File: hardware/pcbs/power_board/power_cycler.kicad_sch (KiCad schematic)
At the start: 6 parts, among them J22 ScrewTerminal_02, Q5 IRFR5305

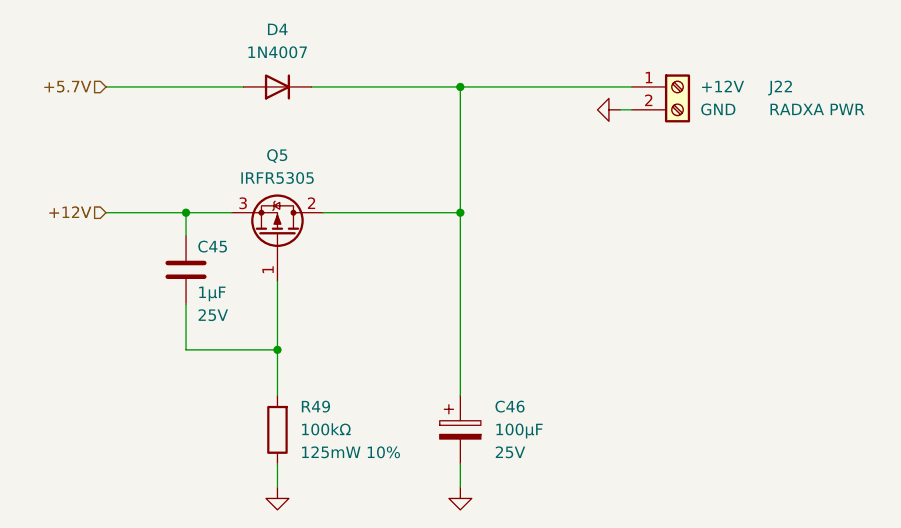
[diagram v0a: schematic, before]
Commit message: power_board: finalise isolated chargers and place USB3 passthrough
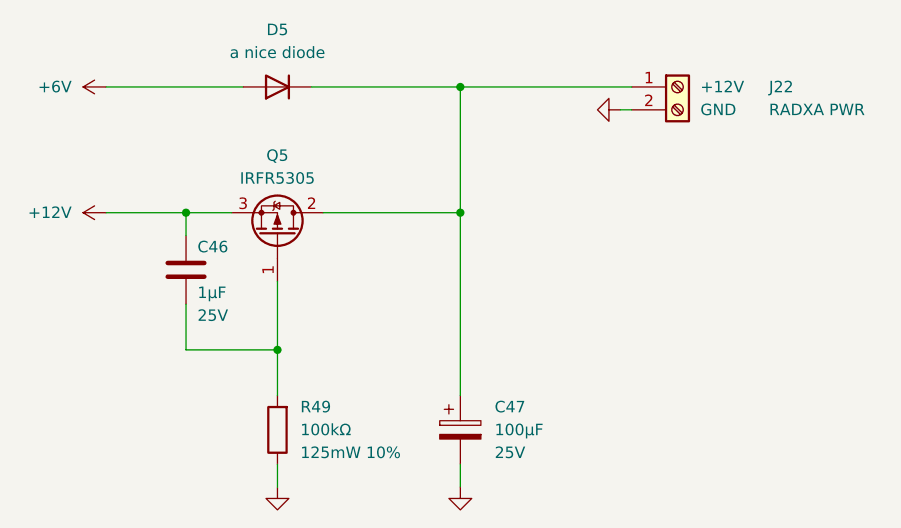
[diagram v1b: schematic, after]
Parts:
- D5: renamed from D4; value 1N4007 -> a nice diode; footprint Diode_THT:D_DO-41_SOD81_P10.16mm_Horizontal -> Diode_SMD:D_SMC; Shop (none) -> TODO
- renumbered C45 to C46, C46 to C47
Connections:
- net +5.7V renamed +6V
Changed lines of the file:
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@@
-		)
-	)
-	(hierarchical_label "+5.7V"
-		(shape input)
-		(at 110.49 71.12 180)
-		(fields_autoplaced yes)
-		(effects
-			(font
-				(size 1.27 1.27)
-			)
-			(justify right)
-		)
-	)
-	(hierarchical_label "+12V"
-		(shape input)
-		(at 110.49 85.09 180)
-		(fields_autoplaced yes)
-		(effects
-			(font
-				(size 1.27 1.27)
-			)
-			(justify right)
 		)
 	)
@@
 		(on_board yes)
 		(dnp no)
-		(property "Reference" "C45"
+		(property "Reference" "C46"
 			(at 120.65 88.9 0)
 			(effects
@@
 			(project "power_board"
 				(path "/4b166175-80a4-48c6-994d-6e62a6160b87/bf145c4c-69aa-4291-854e-cae968acbb49"
-					(reference "C45")
+					(reference "C46")
 					(unit 1)
 				)
@@
 		(dnp no)
 		(fields_autoplaced yes)
-		(property "Reference" "#PWR0111"
+		(property "Reference" "#PWR0110"
 			(at 161.29 73.66 0)
 			(effects
@@
 			(project "power_board"
 				(path "/4b166175-80a4-48c6-994d-6e62a6160b87/bf145c4c-69aa-4291-854e-cae968acbb49"
-					(reference "#PWR0111")
+					(reference "#PWR0110")
 					(unit 1)
 				)
@@
 		(dnp no)
 		(fields_autoplaced yes)
-		(property "Reference" "#PWR0109"
+		(property "Reference" "#PWR0108"
 			(at 129.54 121.92 0)
 			(effects
@@
 			(project "power_board"
 				(path "/4b166175-80a4-48c6-994d-6e62a6160b87/bf145c4c-69aa-4291-854e-cae968acbb49"
-					(reference "#PWR0109")
+					(reference "#PWR0108")
 					(unit 1)
 				)
@@
 		(dnp no)
 		(fields_autoplaced yes)
-		(property "Reference" "D4"
+		(property "Reference" "D5"
 			(at 129.54 64.77 0)
 			(effects
@@
 			)
 		)
-		(property "Value" "1N4007"
+		(property "Value" "a nice diode"
 			(at 129.54 67.31 0)
 			(effects
@@
 			)
 		)
-		(property "Footprint" "Diode_THT:D_DO-41_SOD81_P10.16mm_Horizontal"
+		(property "Footprint" "Diode_SMD:D_SMC"
 			(at 129.54 66.675 0)
 			(effects
@@
 			)
 		)
+		(property "Shop" "TODO"
+			(at 129.54 71.12 0)
+			(effects
+				(font
+					(size 1.27 1.27)
+				)
+				(hide yes)
+			)
+		)
 		(pin "2"
 		)
@@
 			(project "power_board"
 				(path "/4b166175-80a4-48c6-994d-6e62a6160b87/bf145c4c-69aa-4291-854e-cae968acbb49"
-					(reference "D4")
+					(reference "D5")
 					(unit 1)
 				)
@@
 		(on_board yes)
 		(dnp no)
-		(property "Reference" "C46"
+		(property "Reference" "C47"
 			(at 153.67 106.68 0)
 			(effects
@@
 			(project "power_board"
 				(path "/4b166175-80a4-48c6-994d-6e62a6160b87/bf145c4c-69aa-4291-854e-cae968acbb49"
-					(reference "C46")
+					(reference "C47")
 					(unit 1)
 				)
@@
 		(dnp no)
 		(fields_autoplaced yes)
-		(property "Reference" "#PWR0110"
+		(property "Reference" "#PWR0109"
 			(at 149.86 121.92 0)
 			(effects
@@
 			(project "power_board"
 				(path "/4b166175-80a4-48c6-994d-6e62a6160b87/bf145c4c-69aa-4291-854e-cae968acbb49"
-					(reference "#PWR0110")
+					(reference "#PWR0109")
+					(unit 1)
+				)
+			)
+		)
+	)
+	(symbol
+		(lib_id "power:+12V")
+		(at 110.49 85.09 90)
+		(unit 1)
+		(exclude_from_sim no)
+		(in_bom yes)
+		(on_board yes)
+		(dnp no)
+		(fields_autoplaced yes)
+		(property "Reference" "#PWR0107"
+			(at 114.3 85.09 0)
+			(effects
+				(font
+					(size 1.27 1.27)
+				)
+				(hide yes)
+			)
+		)
+		(property "Value" "+12V"
+			(at 106.68 85.0899 90)
+			(effects
+				(font
+					(size 1.27 1.27)
+				)
+				(justify left)
+			)
+		)
+		(property "Footprint" ""
+			(at 110.49 85.09 0)
+			(effects
+				(font
+					(size 1.27 1.27)
+				)
+				(hide yes)
+			)
+		)
+		(property "Datasheet" ""
+			(at 110.49 85.09 0)
+			(effects
+				(font
+					(size 1.27 1.27)
+				)
+				(hide yes)
+			)
+		)
+		(property "Description" "Power symbol creates a global label with name \"+12V\""
+			(at 110.49 85.09 0)
+			(effects
+				(font
+					(size 1.27 1.27)
+				)
+				(hide yes)
+			)
+		)
+		(pin "1"
+		)
+		(instances
+			(project "power_board"
+				(path "/4b166175-80a4-48c6-994d-6e62a6160b87/bf145c4c-69aa-4291-854e-cae968acbb49"
+					(reference "#PWR0107")
 					(unit 1)
 				)
@@
 					(unit 1)
 				)
+			)
+		)
+	)
+	(symbol
+		(lib_id "power:+6V")
+		(at 110.49 71.12 90)
+		(unit 1)
+		(exclude_from_sim no)
+		(in_bom yes)
+		(on_board yes)
+		(dnp no)
+		(fields_autoplaced yes)
+		(property "Reference" "#PWR0106"
+			(at 114.3 71.12 0)
+			(effects
+				(font
+					(size 1.27 1.27)
+				)
+				(hide yes)
+			)
+		)
+		(property "Value" "+6V"
+			(at 106.68 71.1199 90)
+			(effects
+				(font
+					(size 1.27 1.27)
+				)
+				(justify left)
+			)
+		)
+		(property "Footprint" ""
+			(at 110.49 71.12 0)
+			(effects
+				(font
+					(size 1.27 1.27)
+				)
+				(hide yes)
+			)
+		)
+		(property "Datasheet" ""
+			(at 110.49 71.12 0)
+			(effects
+				(font
+					(size 1.27 1.27)
+				)
+				(hide yes)
+			)
+		)
+		(property "Description" "Power symbol creates a global label with name \"+6V\""
+			(at 110.49 71.12 0)
+			(effects
+				(font
+					(size 1.27 1.27)
+				)
+				(hide yes)
+			)
+		)
+		(pin "1"
+		)
+		(instances
+			(project "power_board"
+				(path "/4b166175-80a4-48c6-994d-6e62a6160b87/bf145c4c-69aa-4291-854e-cae968acbb49"
+					(reference "#PWR0106")
+					(unit 1)
+				)

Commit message: power_board: arrange stuff on board
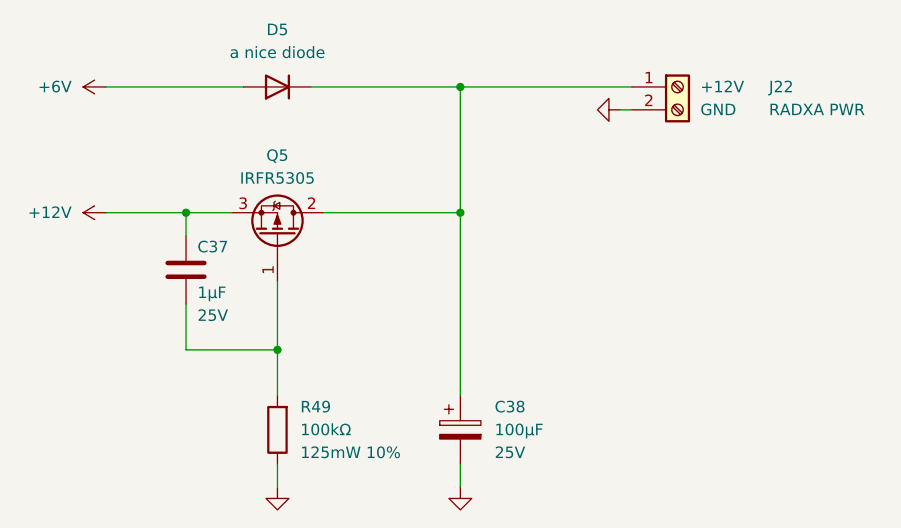
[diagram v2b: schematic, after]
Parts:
- D5: footprint Diode_SMD:D_SMC -> Diode_SMD:D_SMB; Shop TODO -> https://store.comet.bg/Catalogue/Product/48275/
- renumbered C46 to C37, C47 to C38
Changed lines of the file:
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@@
 		(on_board yes)
 		(dnp no)
-		(property "Reference" "C46"
+		(property "Reference" "C37"
 			(at 120.65 88.9 0)
 			(effects
@@
 			(project "power_board"
 				(path "/4b166175-80a4-48c6-994d-6e62a6160b87/bf145c4c-69aa-4291-854e-cae968acbb49"
-					(reference "C46")
+					(reference "C37")
 					(unit 1)
 				)
@@
 		(dnp no)
 		(fields_autoplaced yes)
-		(property "Reference" "#PWR0110"
+		(property "Reference" "#PWR097"
 			(at 161.29 73.66 0)
 			(effects
@@
 			(project "power_board"
 				(path "/4b166175-80a4-48c6-994d-6e62a6160b87/bf145c4c-69aa-4291-854e-cae968acbb49"
-					(reference "#PWR0110")
+					(reference "#PWR097")
 					(unit 1)
 				)
@@
 		(dnp no)
 		(fields_autoplaced yes)
-		(property "Reference" "#PWR0108"
+		(property "Reference" "#PWR095"
 			(at 129.54 121.92 0)
 			(effects
@@
 			(project "power_board"
 				(path "/4b166175-80a4-48c6-994d-6e62a6160b87/bf145c4c-69aa-4291-854e-cae968acbb49"
-					(reference "#PWR0108")
+					(reference "#PWR095")
 					(unit 1)
 				)
@@
 			)
 		)
-		(property "Footprint" "Diode_SMD:D_SMC"
+		(property "Footprint" "Diode_SMD:D_SMB"
 			(at 129.54 66.675 0)
 			(effects
@@
 			)
 		)
-		(property "Shop" "TODO"
+		(property "Shop" "https://store.comet.bg/Catalogue/Product/48275/"
 			(at 129.54 71.12 0)
 			(effects
@@
 		(on_board yes)
 		(dnp no)
-		(property "Reference" "C47"
+		(property "Reference" "C38"
 			(at 153.67 106.68 0)
 			(effects
@@
 			(project "power_board"
 				(path "/4b166175-80a4-48c6-994d-6e62a6160b87/bf145c4c-69aa-4291-854e-cae968acbb49"
-					(reference "C47")
+					(reference "C38")
 					(unit 1)
 				)
@@
 		(dnp no)
 		(fields_autoplaced yes)
-		(property "Reference" "#PWR0109"
+		(property "Reference" "#PWR096"
 			(at 149.86 121.92 0)
 			(effects
@@
 			(project "power_board"
 				(path "/4b166175-80a4-48c6-994d-6e62a6160b87/bf145c4c-69aa-4291-854e-cae968acbb49"
-					(reference "#PWR0109")
+					(reference "#PWR096")
 					(unit 1)
 				)
@@
 		(dnp no)
 		(fields_autoplaced yes)
-		(property "Reference" "#PWR0107"
+		(property "Reference" "#PWR094"
 			(at 114.3 85.09 0)
 			(effects
@@
 			(project "power_board"
 				(path "/4b166175-80a4-48c6-994d-6e62a6160b87/bf145c4c-69aa-4291-854e-cae968acbb49"
-					(reference "#PWR0107")
+					(reference "#PWR094")
 					(unit 1)
 				)
@@
 		(dnp no)
 		(fields_autoplaced yes)
-		(property "Reference" "#PWR0106"
+		(property "Reference" "#PWR093"
 			(at 114.3 71.12 0)
 			(effects
@@
 			(project "power_board"
 				(path "/4b166175-80a4-48c6-994d-6e62a6160b87/bf145c4c-69aa-4291-854e-cae968acbb49"
-					(reference "#PWR0106")
-					(unit 1)
-				)
+					(reference "#PWR093")
+					(unit 1)
+				)

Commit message: power_board: finalise silkscreen
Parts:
- J22: Purpose Pin1 +12V -> RDX
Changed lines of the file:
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@@
 			)
 		)
-		(property "Purpose Pin1" "+12V"
+		(property "Purpose Pin1" "RDX"
 			(at 176.53 71.12 0)
 			(effects

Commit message: power_board: final version
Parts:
- C37: LCSC (none) -> C28323
- D5: value a nice diode -> S2A; LCSC (none) -> C7420368
- R49: LCSC (none) -> C149504
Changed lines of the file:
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@@
+			)
+		)
+		(property "LCSC" "C28323"
+			(at 119.38 91.44 0)
+			(effects
+				(font
+					(size 1.27 1.27)
+				)
+				(hide yes)
 			)
 		)
@@
 		)
 		(property "Shop" "https://store.comet.bg/Catalogue/Product/29105/"
+			(at 129.54 109.22 0)
+			(effects
+				(font
+					(size 1.27 1.27)
+				)
+				(hide yes)
+			)
+		)
+		(property "LCSC" "C149504"
 			(at 129.54 109.22 0)
 			(effects
@@
 			)
 		)
-		(property "Value" "a nice diode"
+		(property "Value" "S2A"
 			(at 129.54 67.31 0)
 			(effects
@@
 			(at 129.54 71.12 0)
 			(effects
+				(font
+					(size 1.27 1.27)
+				)
+				(hide yes)
+			)
+		)
+		(property "LCSC" "C7420368"
+			(at 129.54 71.12 0)
+			(effects

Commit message: power_board: some extra fixes
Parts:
- Q5: LCSC (none) -> C2874618
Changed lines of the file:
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@@
+			)
+		)
+		(property "LCSC" "C2874618"
+			(at 129.54 87.63 0)
+			(effects
+				(font
+					(size 1.27 1.27)
+				)
+				(hide yes)
 			)
 		)
